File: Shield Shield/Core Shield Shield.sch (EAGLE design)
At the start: 6 parts

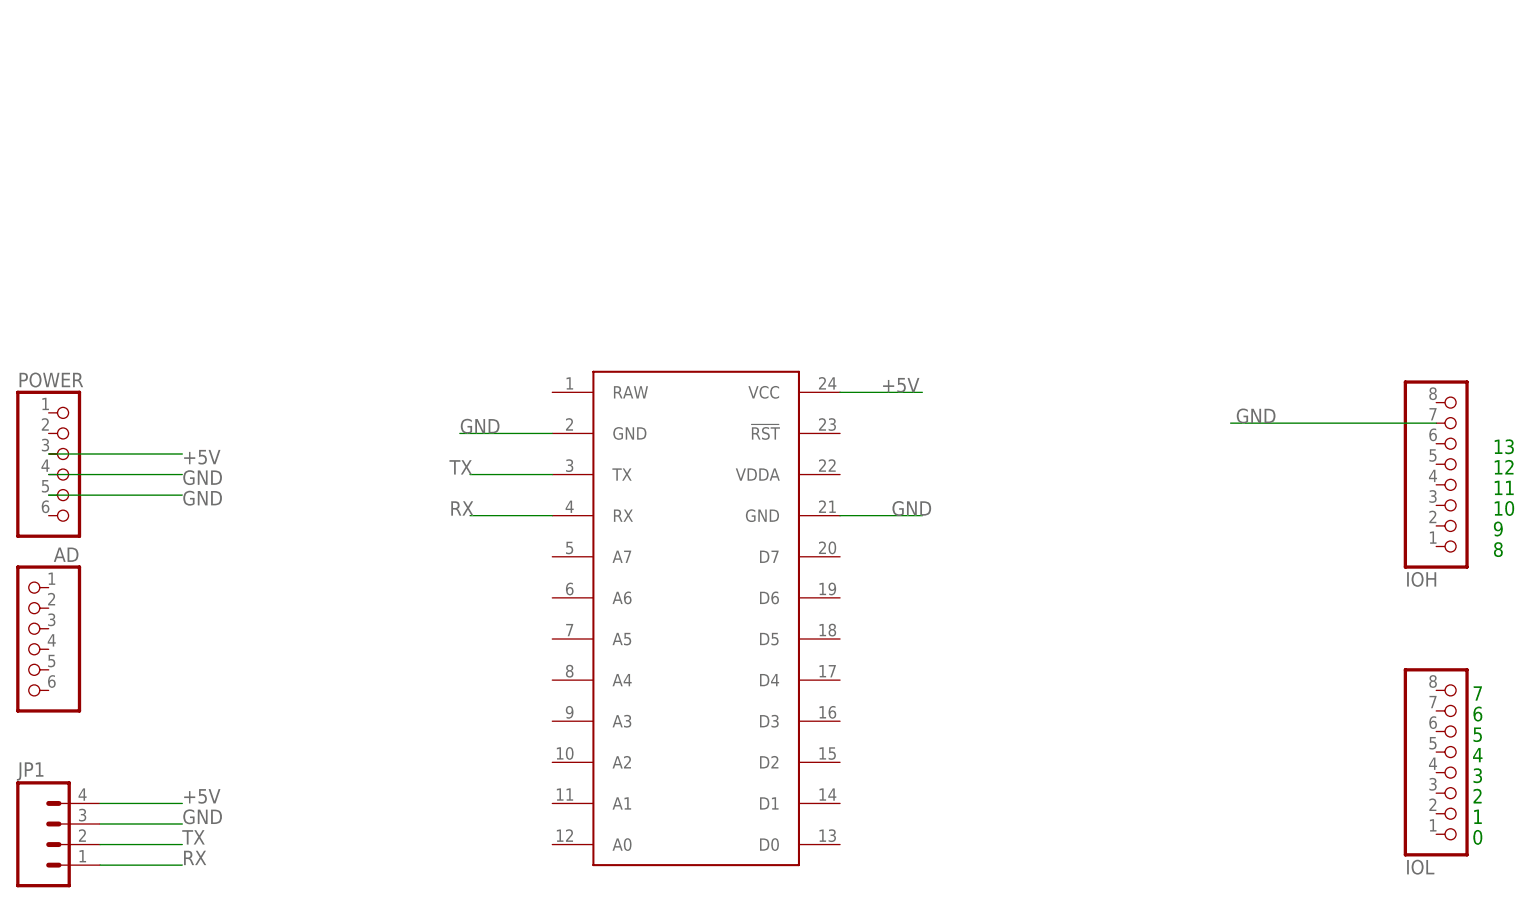
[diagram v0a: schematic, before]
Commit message: Brought in the correct Shield Shield EAGLE files
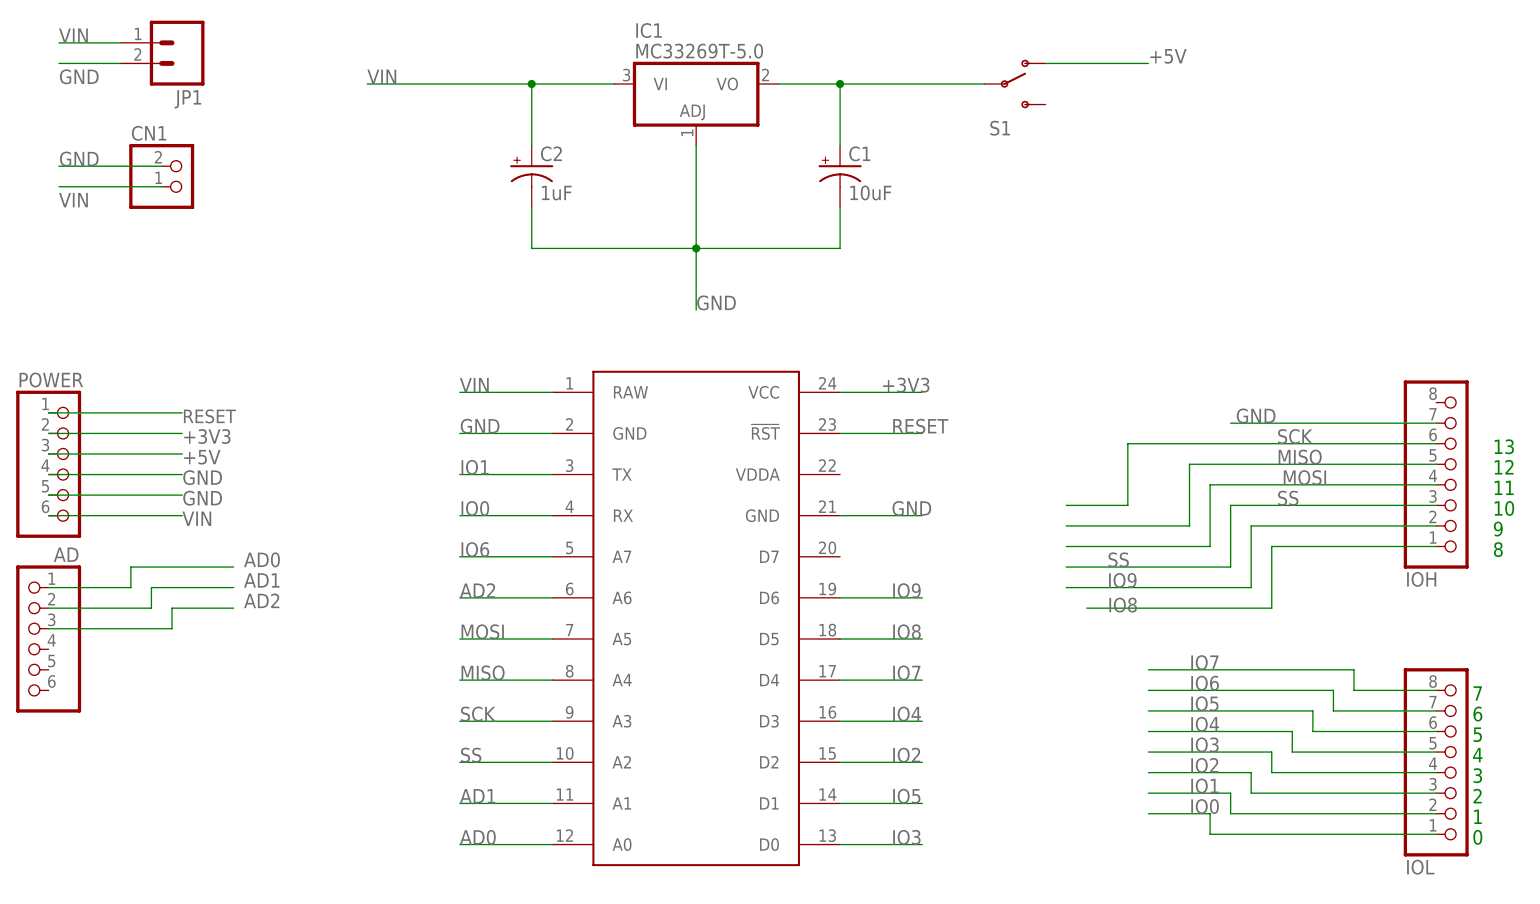
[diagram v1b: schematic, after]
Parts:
- added C1: 10uF, SparkFun-Capacitors:CAP_POLPTH2
- added C2: 1uF, SparkFun-Capacitors:CAP_POLPTH2
- added CN1: (no value), adafruit:JST_2PIN-THM
- added IC1: MC33269T-5.0, linear:MC33269T-5.0
- added S1: (no value), SparkFun-Electromechanical:SWITCH-SPDTPTH
- JP1: device SparkFun-Connectors:M041.27MM -> SparkFun-Connectors:M02LOCK
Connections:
- removed net RX: JP1.1, U$1.RX
- removed net TX: JP1.2, U$1.TX
- new net +3V3: POWER.2, U$1.VCC
- new net AD0: AD.1, U$1.A0
- new net AD1: AD.2, U$1.A1
- new net AD2: AD.3, U$1.A6
- new net IO0: IOL.1, U$1.RX
- new net IO1: IOL.2, U$1.TX
- new net IO2: IOL.3, U$1.D2
- new net IO3: IOL.4, U$1.D0
- new net IO4: IOL.5, U$1.D3
- new net IO5: IOL.6, U$1.D1
- new net IO6: IOL.7, U$1.A7
- new net IO7: IOL.8, U$1.D4
- new net IO8: IOH.1, U$1.D5
- new net IO9: IOH.2, U$1.D6
- new net MISO: IOH.5, U$1.A4
- new net MOSI: IOH.4, U$1.A5
- new net N1: C1.+, IC1.VO, S1.P
- new net RESET: POWER.1, U$1.!RST
- new net SCK: IOH.6, U$1.A3
- new net SS: IOH.3, U$1.A2
- new net VIN: C2.+, CN1.2, IC1.VI, JP1.1, POWER.6, U$1.RAW
- net +5V: now also S1.O; no longer JP1.4, U$1.VCC
- net GND: now also C1.-, C2.-, CN1.1, IC1.ADJ, JP1.2; no longer JP1.3

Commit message: WIP: Created infinity camera from Shield Shield template.
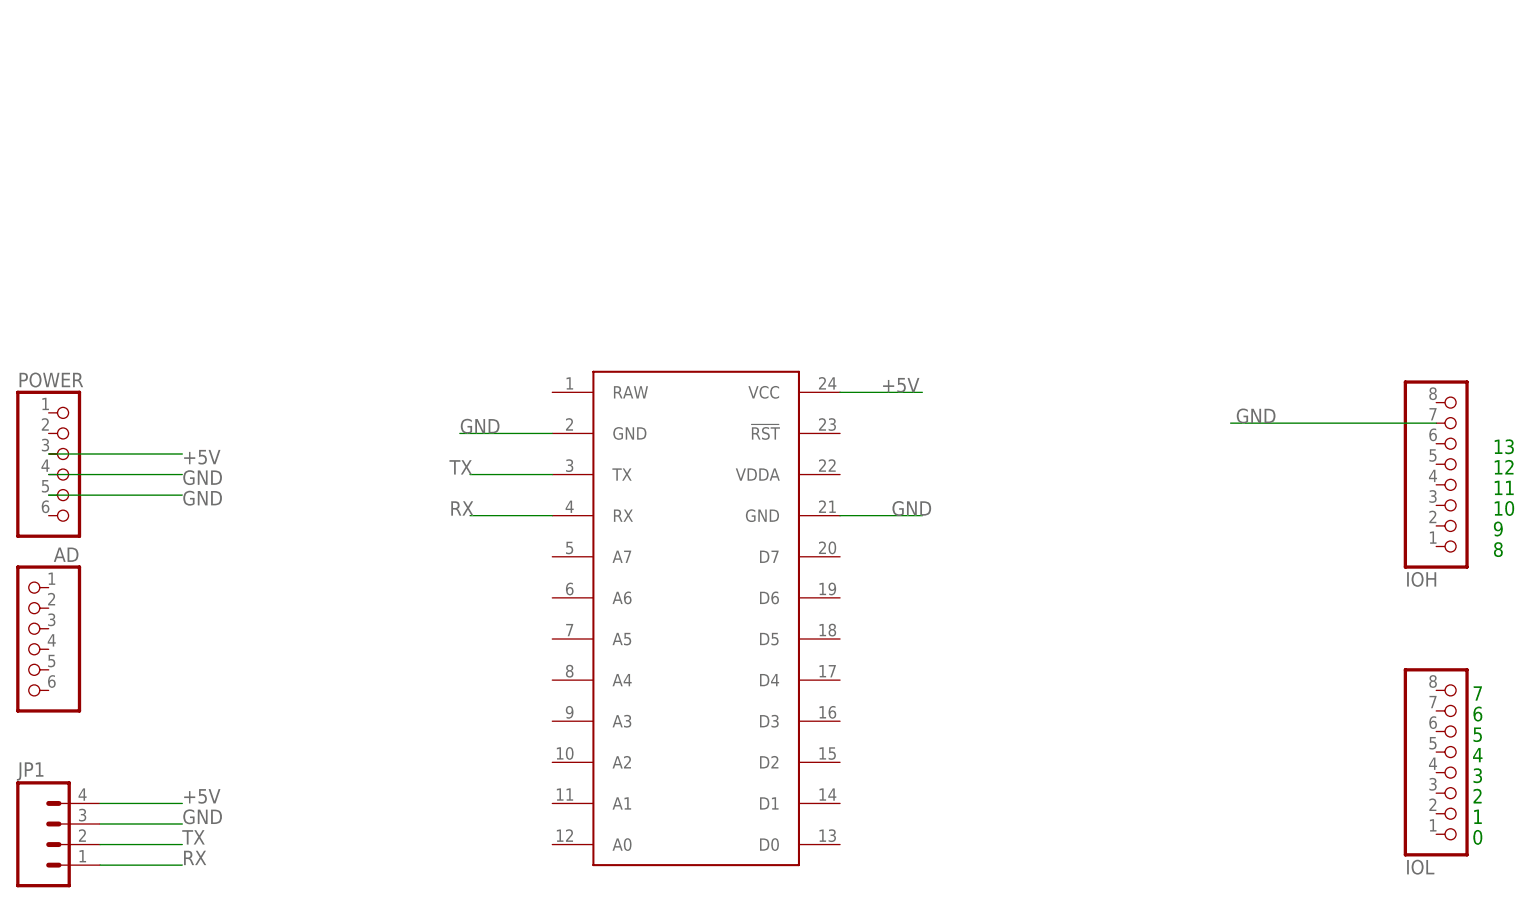
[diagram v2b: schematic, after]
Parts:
- removed C1: 10uF, SparkFun-Capacitors:CAP_POLPTH2
- removed C2: 1uF, SparkFun-Capacitors:CAP_POLPTH2
- removed CN1: (no value), adafruit:JST_2PIN-THM
- removed IC1: MC33269T-5.0, linear:MC33269T-5.0
- removed S1: (no value), SparkFun-Electromechanical:SWITCH-SPDTPTH
- JP1: device SparkFun-Connectors:M02LOCK -> SparkFun-Connectors:M041.27MM
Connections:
- removed net +3V3: POWER.2, U$1.VCC
- removed net AD0: AD.1, U$1.A0
- removed net AD1: AD.2, U$1.A1
- removed net AD2: AD.3, U$1.A6
- removed net IO0: IOL.1, U$1.RX
- removed net IO1: IOL.2, U$1.TX
- removed net IO2: IOL.3, U$1.D2
- removed net IO3: IOL.4, U$1.D0
- removed net IO4: IOL.5, U$1.D3
- removed net IO5: IOL.6, U$1.D1
- removed net IO6: IOL.7, U$1.A7
- removed net IO7: IOL.8, U$1.D4
- removed net IO8: IOH.1, U$1.D5
- removed net IO9: IOH.2, U$1.D6
- removed net MISO: IOH.5, U$1.A4
- removed net MOSI: IOH.4, U$1.A5
- removed net N1: C1.+, IC1.VO, S1.P
- removed net RESET: POWER.1, U$1.!RST
- removed net SCK: IOH.6, U$1.A3
- removed net SS: IOH.3, U$1.A2
- removed net VIN: C2.+, CN1.2, IC1.VI, JP1.1, POWER.6, U$1.RAW
- new net RX: JP1.1, U$1.RX
- new net TX: JP1.2, U$1.TX
- net +5V: now also JP1.4, U$1.VCC; no longer S1.O
- net GND: now also JP1.3; no longer C1.-, C2.-, CN1.1, IC1.ADJ, JP1.2
